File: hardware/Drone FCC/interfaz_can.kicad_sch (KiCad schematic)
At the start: 4 parts, among them J17 Conn_01x04, J18 Conn_01x04, U4 SN65HVD230, U5 SN65HVD230

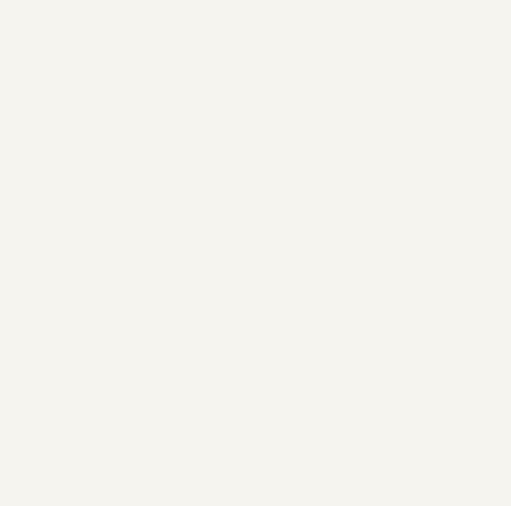
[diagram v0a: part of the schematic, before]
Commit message: all sensors on same schematic subpage
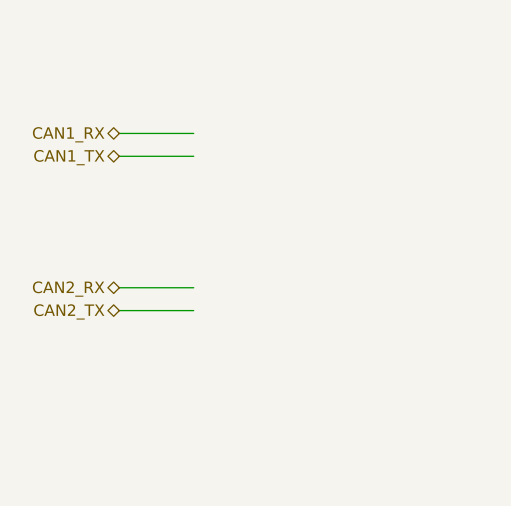
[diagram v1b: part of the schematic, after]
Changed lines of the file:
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@@
+    (stroke (width 0) (type default) (color 0 0 0 0))
+  )
+  (wire (pts (xy 45.085 53.34) (xy 53.34 53.34))
     (stroke (width 0) (type default) (color 0 0 0 0))
   )
@@
     (stroke (width 0) (type default) (color 0 0 0 0))
   )
+  (wire (pts (xy 45.085 67.945) (xy 53.34 67.945))
+    (stroke (width 0) (type default) (color 0 0 0 0))
+  )
+  (wire (pts (xy 45.085 50.8) (xy 53.34 50.8))
+    (stroke (width 0) (type default) (color 0 0 0 0))
+  )
+  (wire (pts (xy 45.085 70.485) (xy 53.34 70.485))
+    (stroke (width 0) (type default) (color 0 0 0 0))
+  )
   (global_label "5V" (shape input) (at 158.115 80.645 0) (fields_autoplaced)
     (effects (font (size 1.27 1.27)) (justify left))
@@
     )
   )
+  (hierarchical_label "CAN2_TX" (shape bidirectional) (at 45.085 70.485 180)
+    (effects (font (size 1.27 1.27)) (justify right))
+  )
+  (hierarchical_label "CAN1_TX" (shape bidirectional) (at 45.085 53.34 180)
+    (effects (font (size 1.27 1.27)) (justify right))
+  )
+  (hierarchical_label "CAN1_RX" (shape bidirectional) (at 45.085 50.8 180)
+    (effects (font (size 1.27 1.27)) (justify right))
+  )
+  (hierarchical_label "CAN2_RX" (shape bidirectional) (at 45.085 67.945 180)
+    (effects (font (size 1.27 1.27)) (justify right))
+  )
   (symbol (lib_id "Interface_CAN_LIN:SN65HVD230") (at 110.49 54.61 0) (unit 1)

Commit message: DSM: deleted dupont conn, PPM: deleted DF-13 conn
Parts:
- J17, J18: footprint Connector_Hirose:Hirose_DF13C_CL535-0404-8-51_1x04-1MP_P1.25mm_Vertical -> DF13-4P-1.25H:HRS_DF13-4P-1.25H(75)
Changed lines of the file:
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@@
       (effects (font (size 1.27 1.27)) (justify left))
     )
-    (property "Footprint" "Connector_Hirose:Hirose_DF13C_CL535-0404-8-51_1x04-1MP_P1.25mm_Vertical" (id 2) (at 163.83 54.61 0)
+    (property "Footprint" "DF13-4P-1.25H:HRS_DF13-4P-1.25H(75)" (id 2) (at 163.83 54.61 0)
       (effects (font (size 1.27 1.27)) hide)
     )
@@
       (effects (font (size 1.27 1.27)) (justify left))
     )
-    (property "Footprint" "Connector_Hirose:Hirose_DF13C_CL535-0404-8-51_1x04-1MP_P1.25mm_Vertical" (id 2) (at 163.83 95.885 0)
+    (property "Footprint" "DF13-4P-1.25H:HRS_DF13-4P-1.25H(75)" (id 2) (at 163.83 95.885 0)
       (effects (font (size 1.27 1.27)) hide)
     )

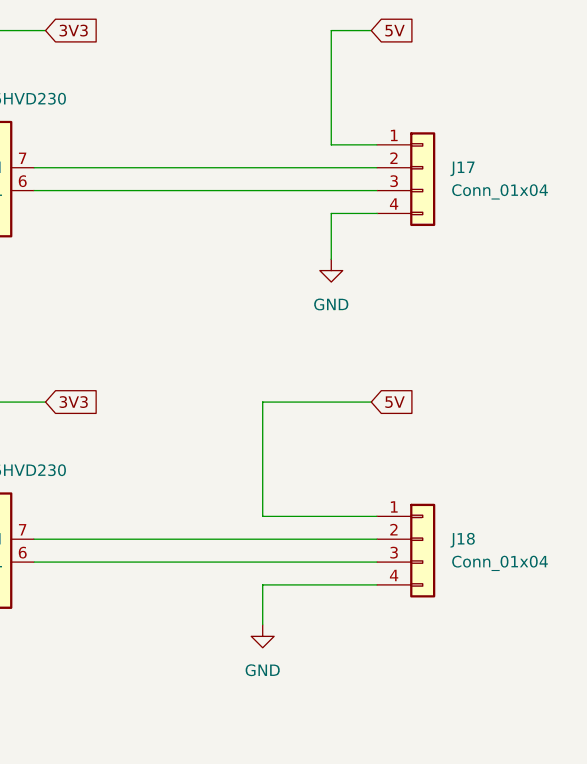
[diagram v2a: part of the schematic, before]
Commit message: add functional schematic for microSD
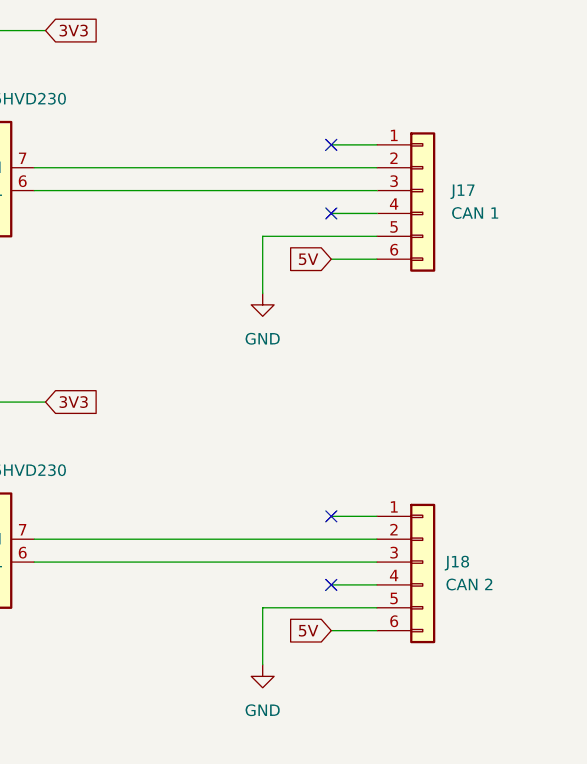
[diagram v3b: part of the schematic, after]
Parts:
- removed J17, J18: Conn_01x04, DF13-4P-1.25H:HRS_DF13-4P-1.25H(75), symbol Connector_Generic:Conn_01x04
- added J17: CAN 1, Connector_Molex:Molex_Micro-Fit_3.0_43045-0600_2x03_P3.00mm_Horizontal, symbol Connector_Generic:Conn_01x06
- added J18: CAN 2, Connector_Molex:Molex_Micro-Fit_3.0_43045-0600_2x03_P3.00mm_Horizontal, symbol Connector_Generic:Conn_01x06
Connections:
- net 5V: now also J17.6 (Pin_6), J18.6 (Pin_6)
- net GND: now also J17.5 (Pin_5), J18.5 (Pin_5)
- net at U4.6 (CANL): now also J17.3 (Pin_3)
- net at U4.7 (CANH): now also J17.2 (Pin_2)
- net at U5.6 (CANL): now also J18.3 (Pin_3)
- net at U5.7 (CANH): now also J18.2 (Pin_2)
- no-connect marks 0 -> 4
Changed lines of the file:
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@@
 (kicad_sch (version 20211123) (generator eeschema)
   (paper "A4")
+  (no_connect (at 153.67 59.69))
+  (no_connect (at 153.67 93.345))
+  (no_connect (at 153.67 52.07))
+  (no_connect (at 153.67 100.965))
+  (wire (pts (xy 153.67 64.77) (xy 158.75 64.77))
+    (stroke (width 0) (type default) (color 0 0 0 0))
+  )
   (wire (pts (xy 110.49 80.645) (xy 110.49 88.265))
     (stroke (width 0) (type default) (color 0 0 0 0))
@@
     (stroke (width 0) (type default) (color 0 0 0 0))
   )
+  (wire (pts (xy 153.67 106.045) (xy 158.75 106.045))
+    (stroke (width 0) (type default) (color 0 0 0 0))
+  )
   (wire (pts (xy 120.65 95.885) (xy 158.75 95.885))
     (stroke (width 0) (type default) (color 0 0 0 0))
   )
-  (wire (pts (xy 158.115 39.37) (xy 153.67 39.37))
-    (stroke (width 0) (type default) (color 0 0 0 0))
-  )
-  (wire (pts (xy 146.05 80.645) (xy 158.115 80.645))
+  (wire (pts (xy 146.05 62.23) (xy 146.05 68.58))
     (stroke (width 0) (type default) (color 0 0 0 0))
   )
@@
     (stroke (width 0) (type default) (color 0 0 0 0))
   )
-  (wire (pts (xy 146.05 93.345) (xy 158.75 93.345))
-    (stroke (width 0) (type default) (color 0 0 0 0))
-  )
   (wire (pts (xy 45.085 53.34) (xy 53.34 53.34))
     (stroke (width 0) (type default) (color 0 0 0 0))
@@
     (stroke (width 0) (type default) (color 0 0 0 0))
   )
-  (wire (pts (xy 153.67 39.37) (xy 153.67 52.07))
-    (stroke (width 0) (type default) (color 0 0 0 0))
-  )
-  (wire (pts (xy 146.05 100.965) (xy 146.05 105.41))
+  (wire (pts (xy 146.05 62.23) (xy 158.75 62.23))
     (stroke (width 0) (type default) (color 0 0 0 0))
   )
@@
     (stroke (width 0) (type default) (color 0 0 0 0))
   )
+  (wire (pts (xy 158.75 93.345) (xy 153.67 93.345))
+    (stroke (width 0) (type default) (color 0 0 0 0))
+  )
+  (wire (pts (xy 153.67 100.965) (xy 158.75 100.965))
+    (stroke (width 0) (type default) (color 0 0 0 0))
+  )
   (wire (pts (xy 110.49 80.645) (xy 121.92 80.645))
     (stroke (width 0) (type default) (color 0 0 0 0))
@@
     (stroke (width 0) (type default) (color 0 0 0 0))
   )
-  (wire (pts (xy 146.05 80.645) (xy 146.05 93.345))
-    (stroke (width 0) (type default) (color 0 0 0 0))
-  )
   (wire (pts (xy 158.75 52.07) (xy 153.67 52.07))
     (stroke (width 0) (type default) (color 0 0 0 0))
   )
-  (wire (pts (xy 158.75 59.69) (xy 153.67 59.69))
-    (stroke (width 0) (type default) (color 0 0 0 0))
-  )
-  (wire (pts (xy 146.05 100.965) (xy 158.75 100.965))
-    (stroke (width 0) (type default) (color 0 0 0 0))
-  )
-  (wire (pts (xy 153.67 59.69) (xy 153.67 64.77))
+  (wire (pts (xy 146.05 103.505) (xy 158.75 103.505))
+    (stroke (width 0) (type default) (color 0 0 0 0))
+  )
+  (wire (pts (xy 146.05 103.505) (xy 146.05 109.855))
     (stroke (width 0) (type default) (color 0 0 0 0))
   )
@@
     (stroke (width 0) (type default) (color 0 0 0 0))
   )
+  (wire (pts (xy 153.67 59.69) (xy 158.75 59.69))
+    (stroke (width 0) (type default) (color 0 0 0 0))
+  )
   (wire (pts (xy 45.085 50.8) (xy 53.34 50.8))
     (stroke (width 0) (type default) (color 0 0 0 0))
@@
     (stroke (width 0) (type default) (color 0 0 0 0))
   )
-  (global_label "5V" (shape input) (at 158.115 80.645 0) (fields_autoplaced)
-    (effects (font (size 1.27 1.27)) (justify left))
-    (property "Intersheet References" "${INTERSHEET_REFS}" (id 0) (at 162.8262 80.5656 0)
-      (effects (font (size 1.27 1.27)) (justify left) hide)
+  (global_label "5V" (shape input) (at 153.67 106.045 180) (fields_autoplaced)
+    (effects (font (size 1.27 1.27)) (justify right))
+    (property "Intersheet References" "${INTERSHEET_REFS}" (id 0) (at 148.9588 106.1244 0)
+      (effects (font (size 1.27 1.27)) (justify right) hide)
     )
   )
@@
     )
   )
-  (global_label "5V" (shape input) (at 158.115 39.37 0) (fields_autoplaced)
-    (effects (font (size 1.27 1.27)) (justify left))
-    (property "Intersheet References" "${INTERSHEET_REFS}" (id 0) (at 162.8262 39.2906 0)
-      (effects (font (size 1.27 1.27)) (justify left) hide)
+  (global_label "5V" (shape input) (at 153.67 64.77 180) (fields_autoplaced)
+    (effects (font (size 1.27 1.27)) (justify right))
+    (property "Intersheet References" "${INTERSHEET_REFS}" (id 0) (at 148.9588 64.8494 0)
+      (effects (font (size 1.27 1.27)) (justify right) hide)
     )
   )
@@
   (hierarchical_label "CAN2_RX" (shape bidirectional) (at 45.085 67.945 180)
     (effects (font (size 1.27 1.27)) (justify right))
+  )
+  (symbol (lib_name "GND_1") (lib_id "power:GND") (at 146.05 68.58 0) (unit 1)
+    (in_bom yes) (on_board yes) (fields_autoplaced)
+    (property "Reference" "#PWR0103" (id 0) (at 146.05 74.93 0)
+      (effects (font (size 1.27 1.27)) hide)
+    )
+    (property "Value" "GND" (id 1) (at 146.05 73.66 0))
+    (property "Footprint" "" (id 2) (at 146.05 68.58 0)
+      (effects (font (size 1.27 1.27)) hide)
+    )
+    (property "Datasheet" "" (id 3) (at 146.05 68.58 0)
+      (effects (font (size 1.27 1.27)) hide)
+    )
+    (pin "1")
   )
   (symbol (lib_id "Interface_CAN_LIN:SN65HVD230") (at 110.49 54.61 0) (unit 1)
@@
     (pin "8")
   )
-  (symbol (lib_id "power:GND") (at 146.05 105.41 0) (unit 1)
-    (in_bom yes) (on_board yes) (fields_autoplaced)
-    (property "Reference" "#PWR0104" (id 0) (at 146.05 111.76 0)
-      (effects (font (size 1.27 1.27)) hide)
-    )
-    (property "Value" "GND" (id 1) (at 146.05 110.49 0))
-    (property "Footprint" "" (id 2) (at 146.05 105.41 0)
-      (effects (font (size 1.27 1.27)) hide)
-    )
-    (property "Datasheet" "" (id 3) (at 146.05 105.41 0)
+  (symbol (lib_name "GND_1") (lib_id "power:GND") (at 146.05 109.855 0) (unit 1)
+    (in_bom yes) (on_board yes) (fields_autoplaced)
+    (property "Reference" "#PWR0104" (id 0) (at 146.05 116.205 0)
+      (effects (font (size 1.27 1.27)) hide)
+    )
+    (property "Value" "GND" (id 1) (at 146.05 114.935 0))
+    (property "Footprint" "" (id 2) (at 146.05 109.855 0)
+      (effects (font (size 1.27 1.27)) hide)
+    )
+    (property "Datasheet" "" (id 3) (at 146.05 109.855 0)
       (effects (font (size 1.27 1.27)) hide)
     )
@@
     (pin "8")
   )
-  (symbol (lib_id "Connector_Generic:Conn_01x04") (at 163.83 54.61 0) (unit 1)
-    (in_bom yes) (on_board yes) (fields_autoplaced)
-    (property "Reference" "J17" (id 0) (at 167.005 54.6099 0)
-      (effects (font (size 1.27 1.27)) (justify left))
-    )
-    (property "Value" "Conn_01x04" (id 1) (at 167.005 57.1499 0)
-      (effects (font (size 1.27 1.27)) (justify left))
-    )
-    (property "Footprint" "DF13-4P-1.25H:HRS_DF13-4P-1.25H(75)" (id 2) (at 163.83 54.61 0)
-      (effects (font (size 1.27 1.27)) hide)
-    )
-    (property "Datasheet" "~" (id 3) (at 163.83 54.61 0)
-      (effects (font (size 1.27 1.27)) hide)
-    )
-    (pin "1")
-    (pin "2")
-    (pin "3")
-    (pin "4")
+  (symbol (lib_id "Connector_Generic:Conn_01x06") (at 163.83 57.15 0) (unit 1)
+    (in_bom yes) (on_board yes) (fields_autoplaced)
+    (property "Reference" "J17" (id 0) (at 167.005 57.1499 0)
+      (effects (font (size 1.27 1.27)) (justify left))
+    )
+    (property "Value" "CAN 1" (id 1) (at 167.005 59.6899 0)
+      (effects (font (size 1.27 1.27)) (justify left))
+    )
+    (property "Footprint" "Connector_Molex:Molex_Micro-Fit_3.0_43045-0600_2x03_P3.00mm_Horizontal" (id 2) (at 163.83 57.15 0)
+      (effects (font (size 1.27 1.27)) hide)
+    )
+    (property "Datasheet" "~" (id 3) (at 163.83 57.15 0)
+      (effects (font (size 1.27 1.27)) hide)
+    )
+    (pin "1")
+    (pin "2")
+    (pin "3")
+    (pin "4")
+    (pin "5")
+    (pin "6")
   )
   (symbol (lib_id "power:GND") (at 110.49 71.12 0) (unit 1)
@@
     (pin "1")
   )
-  (symbol (lib_id "Connector_Generic:Conn_01x04") (at 163.83 95.885 0) (unit 1)
-    (in_bom yes) (on_board yes) (fields_autoplaced)
-    (property "Reference" "J18" (id 0) (at 167.005 95.8849 0)
-      (effects (font (size 1.27 1.27)) (justify left))
-    )
-    (property "Value" "Conn_01x04" (id 1) (at 167.005 98.4249 0)
-      (effects (font (size 1.27 1.27)) (justify left))
-    )
-    (property "Footprint" "DF13-4P-1.25H:HRS_DF13-4P-1.25H(75)" (id 2) (at 163.83 95.885 0)
-      (effects (font (size 1.27 1.27)) hide)
-    )
-    (property "Datasheet" "~" (id 3) (at 163.83 95.885 0)
-      (effects (font (size 1.27 1.27)) hide)
-    )
-    (pin "1")
-    (pin "2")
-    (pin "3")
-    (pin "4")
+  (symbol (lib_id "Connector_Generic:Conn_01x06") (at 163.83 98.425 0) (unit 1)
+    (in_bom yes) (on_board yes) (fields_autoplaced)
+    (property "Reference" "J18" (id 0) (at 166.37 98.4249 0)
+      (effects (font (size 1.27 1.27)) (justify left))
+    )
+    (property "Value" "CAN 2" (id 1) (at 166.37 100.9649 0)
+      (effects (font (size 1.27 1.27)) (justify left))
+    )
+    (property "Footprint" "Connector_Molex:Molex_Micro-Fit_3.0_43045-0600_2x03_P3.00mm_Horizontal" (id 2) (at 163.83 98.425 0)
+      (effects (font (size 1.27 1.27)) hide)
+    )
+    (property "Datasheet" "~" (id 3) (at 163.83 98.425 0)
+      (effects (font (size 1.27 1.27)) hide)
+    )
+    (pin "1")
+    (pin "2")
+    (pin "3")
+    (pin "4")
+    (pin "5")
+    (pin "6")
   )
   (symbol (lib_id "power:GND") (at 110.49 112.395 0) (unit 1)
@@
       (effects (font (size 1.27 1.27)) hide)
     )
-    (pin "1")
-  )
-  (symbol (lib_id "power:GND") (at 153.67 64.77 0) (unit 1)
-    (in_bom yes) (on_board yes) (fields_autoplaced)
-    (property "Reference" "#PWR0103" (id 0) (at 153.67 71.12 0)
-      (effects (font (size 1.27 1.27)) hide)
-    )
-    (property "Value" "GND" (id 1) (at 153.67 69.85 0))
-    (property "Footprint" "" (id 2) (at 153.67 64.77 0)
-      (effects (font (size 1.27 1.27)) hide)
-    )
-    (property "Datasheet" "" (id 3) (at 153.67 64.77 0)
-      (effects (font (size 1.27 1.27)) hide)
-    )
